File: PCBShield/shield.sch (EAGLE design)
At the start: 75 parts, among them IC1 L293D, IC3 LD117AV

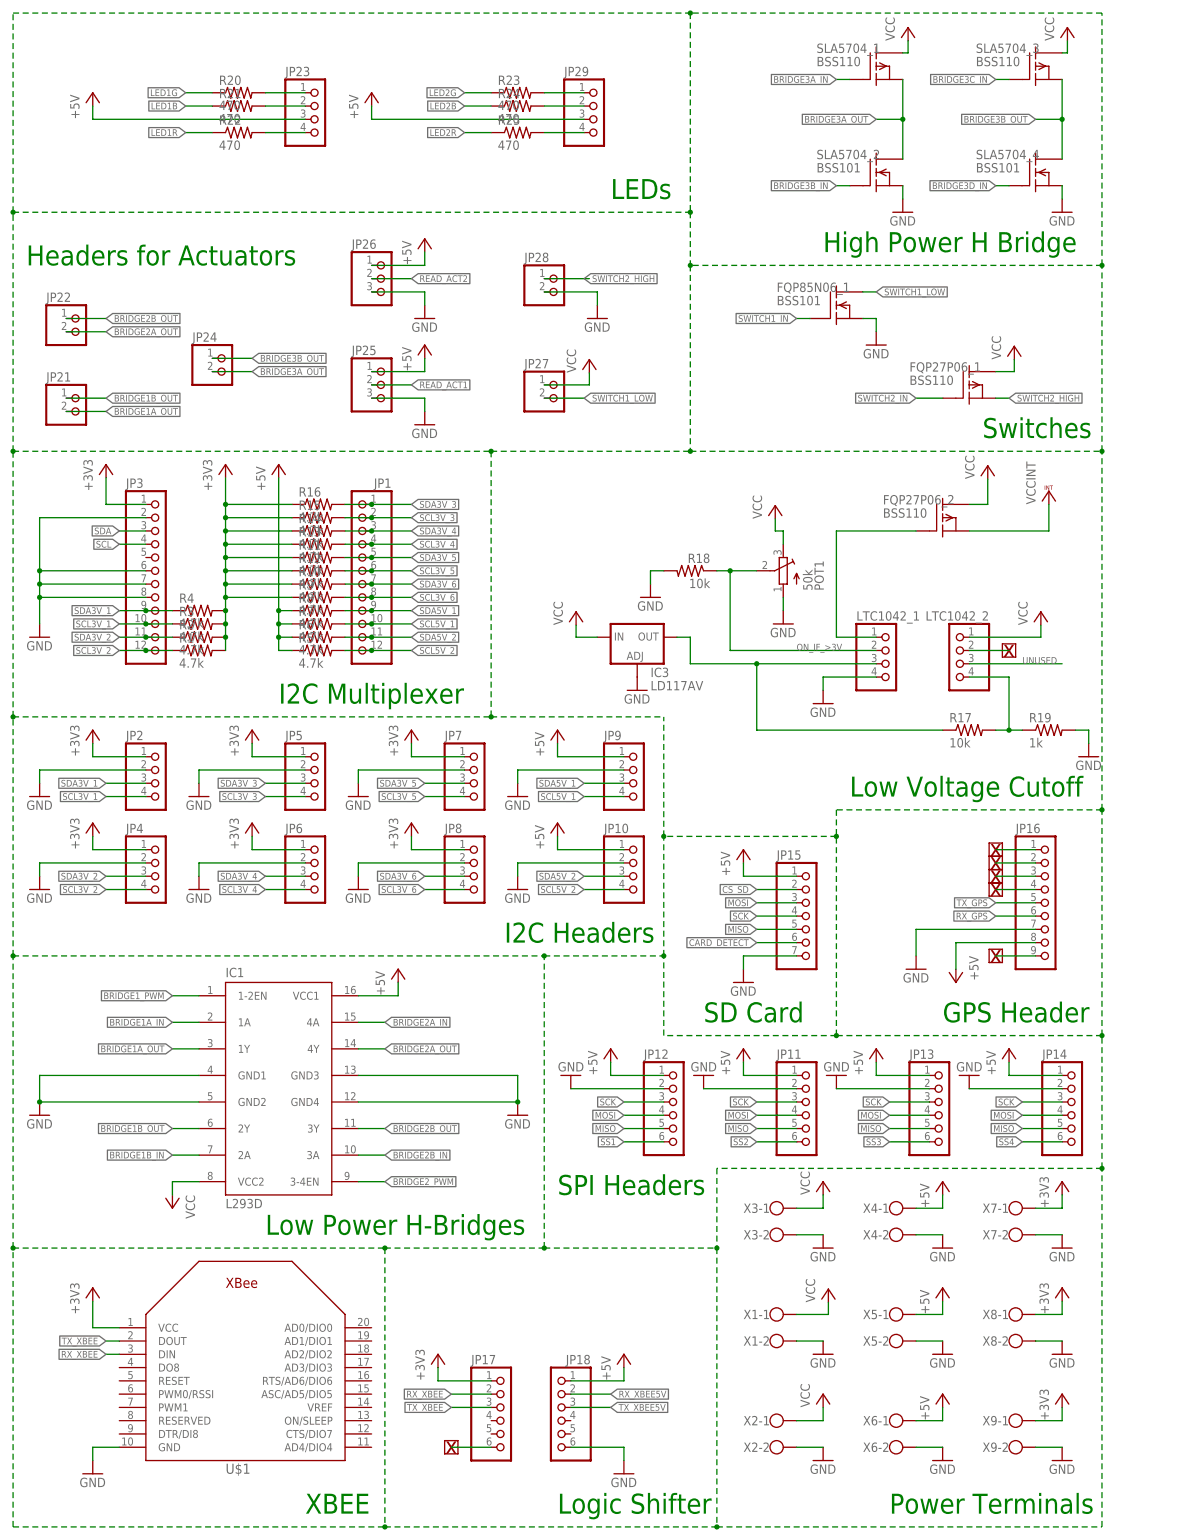
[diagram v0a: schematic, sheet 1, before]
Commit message: Now all custom parts have been created for the printed circuit board so actual board design can begin smoothly
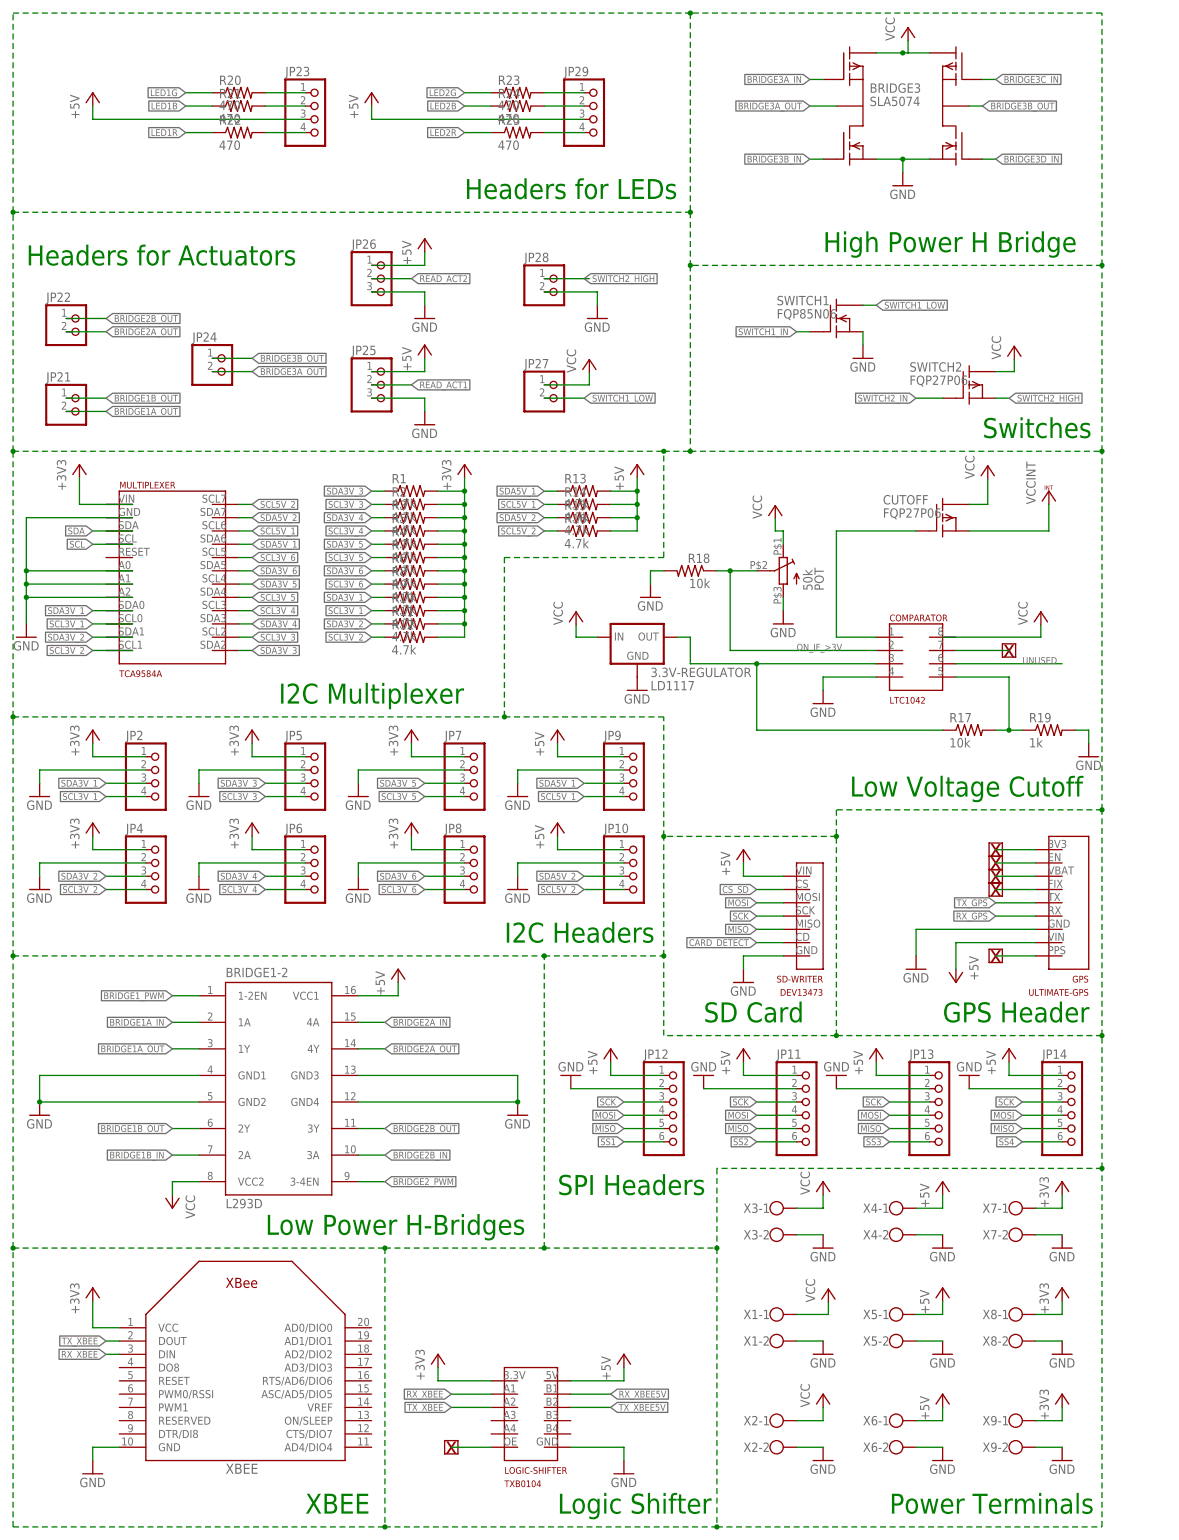
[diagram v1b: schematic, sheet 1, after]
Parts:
- removed FQP27P06_1, FQP27P06_2, SLA5704_1, SLA5704_3: BSS110, transistor-fet:BSS110
- removed FQP85N06_1, SLA5704_2, SLA5704_4: BSS101, transistor-fet:BSS101
- removed IC3: LD117AV, v-reg:LD117AV
- removed JP1, JP3: (no value), microbuilder:HEADER-1X12
- removed JP15: (no value), pinhead:PINHD-1X7
- removed JP16: (no value), pinhead:PINHD-1X9
- removed JP17, JP18: (no value), pinhead:PINHD-1X6
- removed LTC1042_1, LTC1042_2: (no value), pinhead:PINHD-1X4
- removed POT1: 50k, adafruit:TRIMPOT3386
- added 3.3V-REGULATOR: LD1117, specialparts:LD1117
- added BRIDGE3: SLA5074, specialparts:SLA5074
- added COMPARATOR: LTC1042, specialparts:LTC1042
- added CUTOFF, SWITCH2: FQP27P06, specialparts:FQP27P06
- added GPS: ULTIMATE-GPS, specialparts:ULTIMATE-GPS
- added LOGIC-SHIFTER: TXB0104, specialparts:TXB0104
- added MULTIPLEXER: TCA9584A, specialparts:TCA9584A
- added POT: 50k, specialparts:PV37W503C01B00
- added SD-WRITER: DEV13473, specialparts:DEV13473
- added SWITCH1: FQP85N06, specialparts:FQP85N06
- renumbered IC1 to BRIDGE1-2, U$1 to XBEE
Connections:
- removed net CARD_DETECT: JP15.6
- removed net N$10: JP16.2
- removed net N$11: JP16.3
- removed net N$12: JP16.4
- removed net N$13: JP17.6
- removed net N$15: LTC1042_2.2
- removed net N$17: JP16.9
- removed net N$9: JP16.1
- removed net UNUSED: LTC1042_2.3
- net +3V3: now also MULTIPLEXER.VIN, R10.2, R11.2, R12.2, R5.2, R6.2, R7.2, R8.2, R9.2; no longer JP17.1, JP3.1, R10.1, R11.1, R12.1, R13.1, R14.1, R15.1, R16.1, R9.1
- net +5V: now also R13.2, R14.2, R15.2, R16.2; no longer JP15.1, JP16.8, JP18.1, R5.1, R6.1, R7.1, R8.1
- net BRIDGE3A_IN: now also BRIDGE3.P$4; no longer SLA5704_1.G
- net BRIDGE3A_OUT: now also BRIDGE3.P$3; no longer SLA5704_1.S, SLA5704_2.D
- net BRIDGE3B_IN: now also BRIDGE3.P$2; no longer SLA5704_2.G
- net BRIDGE3B_OUT: now also BRIDGE3.P$7; no longer SLA5704_3.S, SLA5704_4.D
- net BRIDGE3C_IN: now also BRIDGE3.P$9; no longer SLA5704_3.G
- net BRIDGE3D_IN: now also BRIDGE3.P$6; no longer SLA5704_4.G
- net CS_SD: no longer JP15.2
- net GND: now also BRIDGE3.P$1, BRIDGE3.P$8, MULTIPLEXER.A0, MULTIPLEXER.A1, MULTIPLEXER.A2, MULTIPLEXER.GND, POT.P$3, SWITCH1.S; no longer FQP85N06_1.S, IC3.ADJ, JP15.7, JP16.7, JP18.6, JP3.2, JP3.6, JP3.7, JP3.8, LTC1042_1.4, POT1.A, SLA5704_2.S, SLA5704_4.S
- net MISO: no longer JP15.5
- net MOSI: no longer JP15.3
- net N$16: no longer LTC1042_2.4
- net N$18: now also CUTOFF.G; no longer FQP27P06_2.G, LTC1042_1.1
- net N$19: now also 3.3V-REGULATOR.VOUT; no longer IC3.OUT, LTC1042_1.3
- net ON_IF_>3V: now also POT.P$2; no longer LTC1042_1.2, POT1.S
- net RX_GPS: no longer JP16.6
- net RX_XBEE: no longer JP17.2
- net RX_XBEE5V: no longer JP18.2
- net SCK: no longer JP15.4
- net SCL: now also MULTIPLEXER.SCL; no longer JP3.4
- net SCL3V_1: now also MULTIPLEXER.SCL0, R10.1; no longer JP3.10, R3.1
- net SCL3V_2: now also MULTIPLEXER.SCL1, R12.1; no longer JP3.12, R1.1
- net SCL3V_3: now also R2.1; no longer JP1.2, R15.2
- net SCL3V_4: now also R5.1; no longer JP1.4, R13.2
- net SCL3V_5: now also R7.1; no longer JP1.6, R12.2
- net SCL3V_6: now also R8.1; no longer JP1.8, R9.2
- net SCL5V_1: now also R14.1; no longer JP1.10, R7.2
- net SCL5V_2: now also R16.1; no longer JP1.12, R5.2
- net SDA: now also MULTIPLEXER.SDA; no longer JP3.3
- net SDA3V_1: now also MULTIPLEXER.SDA0, R9.1; no longer JP3.9, R4.1
- net SDA3V_2: now also MULTIPLEXER.SDA1, R11.1; no longer JP3.11, R2.1
- net SDA3V_3: now also R1.1; no longer JP1.1, R16.2
- net SDA3V_4: now also R3.1; no longer JP1.3, R14.2
- net SDA3V_5: now also R4.1; no longer JP1.5, R11.2
- net SDA3V_6: now also R6.1; no longer JP1.7, R10.2
- net SDA5V_1: now also R13.1; no longer JP1.9, R8.2
- net SDA5V_2: now also R15.1; no longer JP1.11, R6.2
- net SWITCH1_IN: no longer FQP85N06_1.G
- net SWITCH1_LOW: no longer FQP85N06_1.D
- net SWITCH2_HIGH: now also SWITCH2.S; no longer FQP27P06_1.S
- net SWITCH2_IN: now also SWITCH2.G; no longer FQP27P06_1.G
- net TX_GPS: no longer JP16.5
- net TX_XBEE: no longer JP17.3
- net TX_XBEE5V: no longer JP18.3
- net VCC: now also 3.3V-REGULATOR.VIN, BRIDGE3.P$10, BRIDGE3.P$5, CUTOFF.D, POT.P$1, SWITCH2.D; no longer FQP27P06_1.D, FQP27P06_2.D, IC3.IN, LTC1042_2.1, POT1.E, SLA5704_1.D, SLA5704_3.D
- net VCCINT: now also CUTOFF.S; no longer FQP27P06_2.S
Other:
- note added: "Headers for LEDs"
- note removed: "LEDs"
- moved on the sheet: R1, R10, R11, R12, R13, R14, R15, R16, R2, R3, R4, R5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

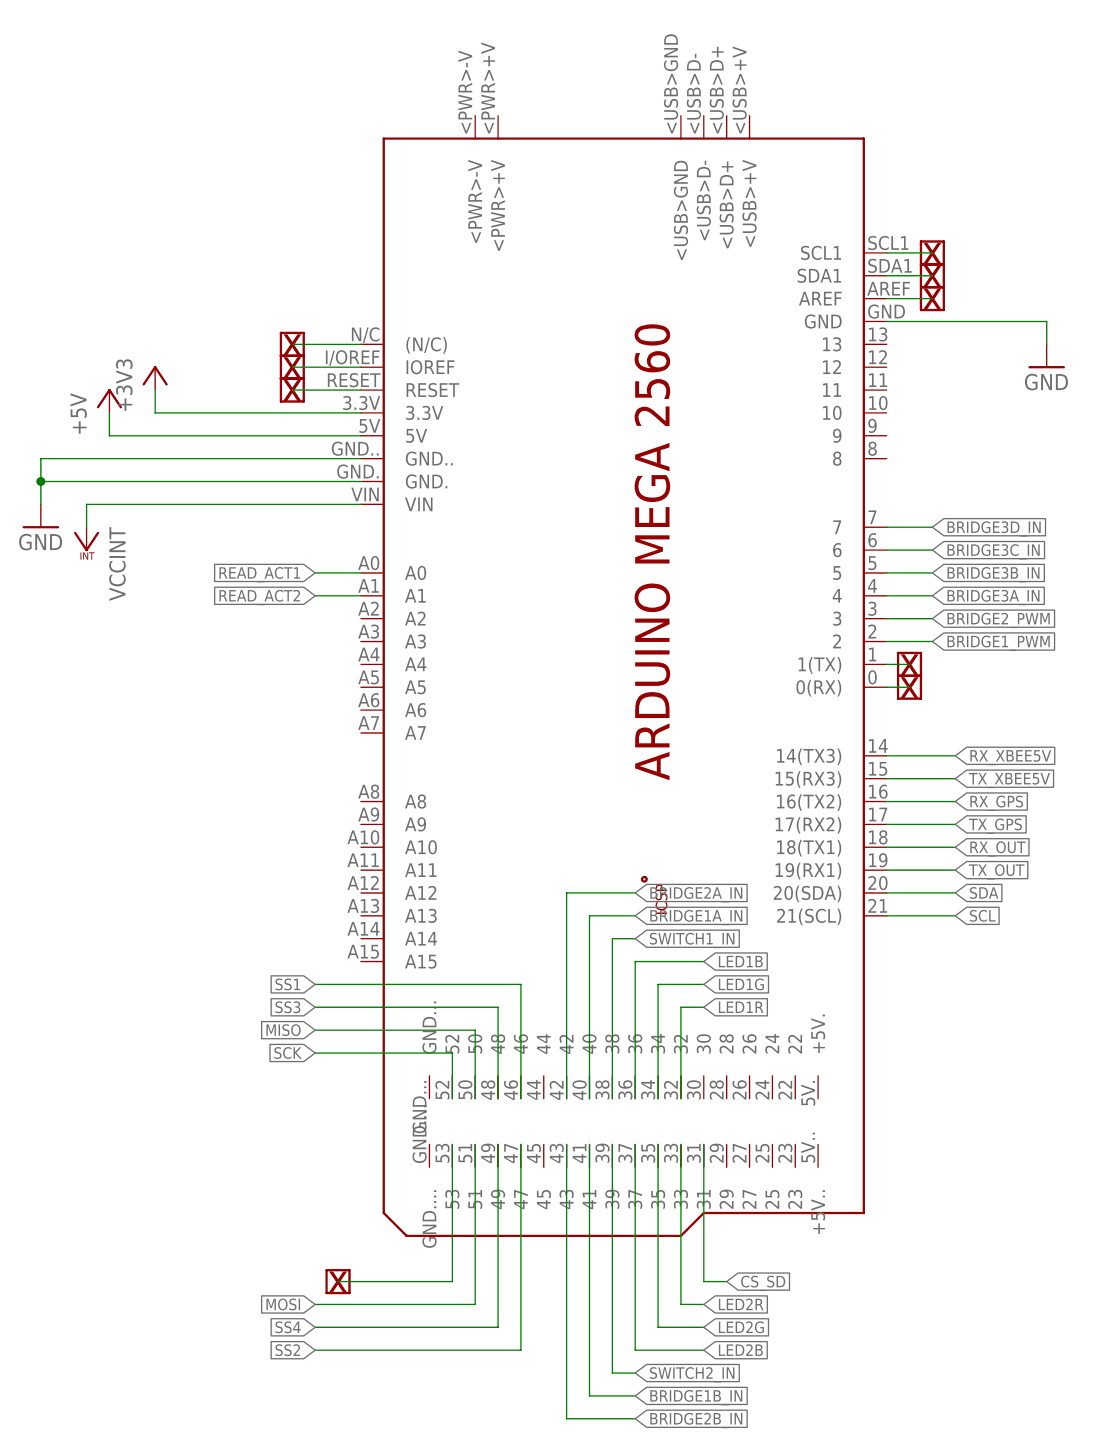
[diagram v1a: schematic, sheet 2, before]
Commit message: Revised board design to include only pins needed for a shield (no ISP header or USB/POWER). Added hole for reset switch
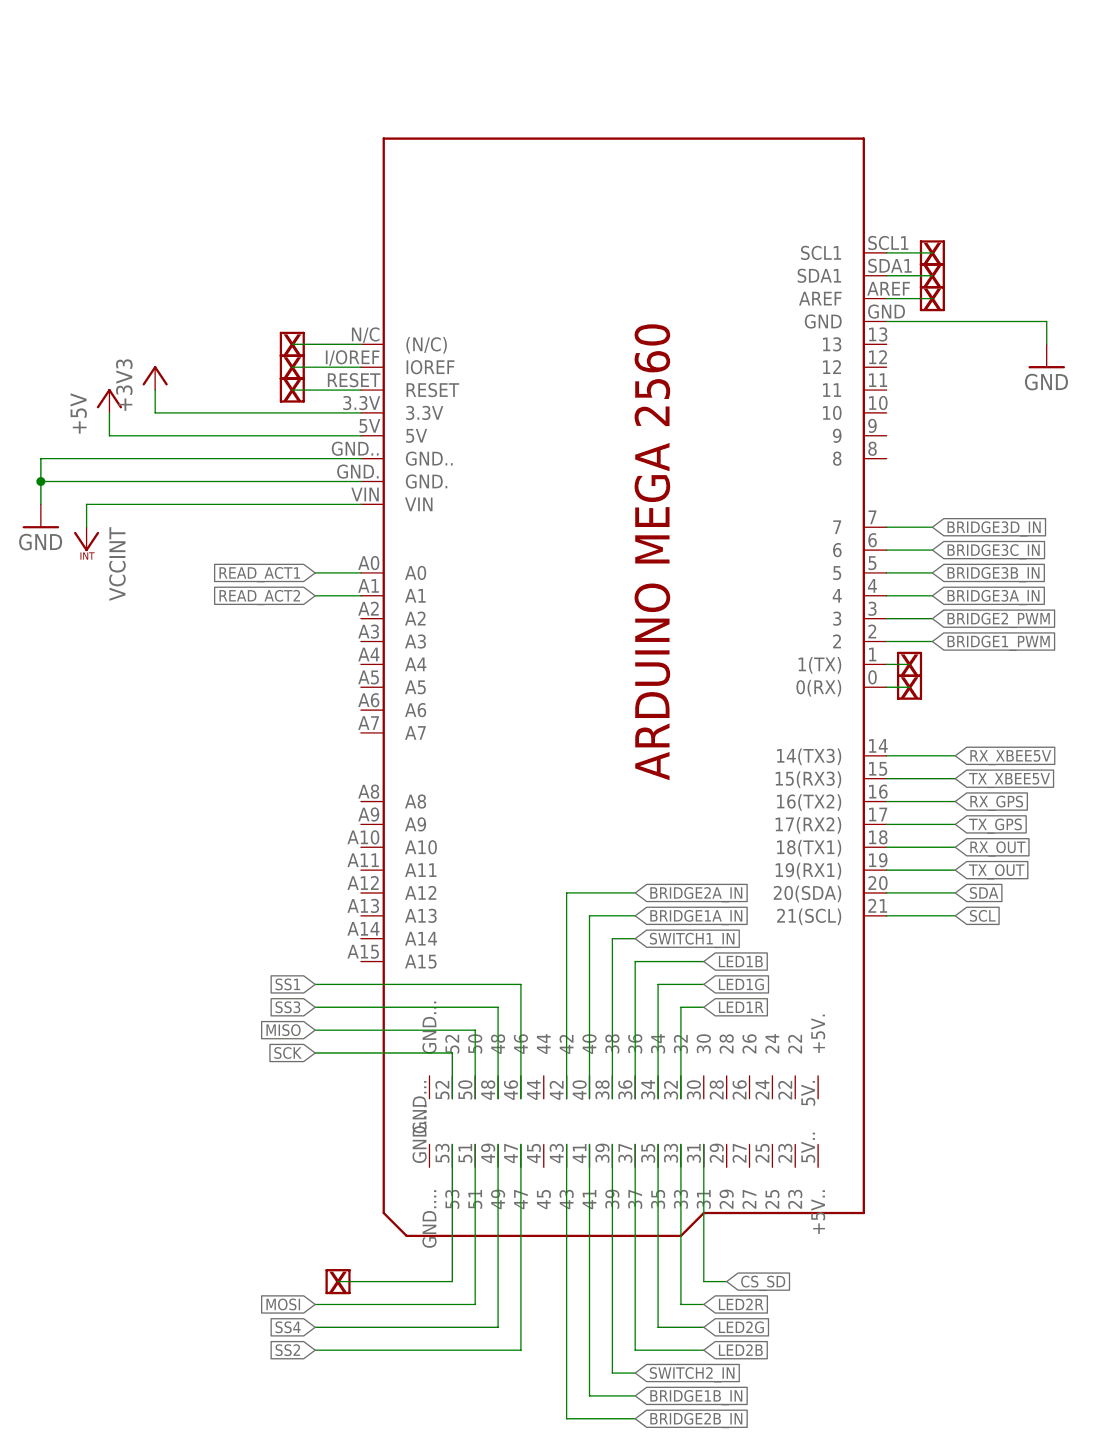
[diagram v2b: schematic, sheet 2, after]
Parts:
- removed PCB1: ARDUINO_MEGA2560, E14_Arduino_revC:ARDUINO_MEGA2560
- added PCB2: ARDUINO_MEGA2560_SHIELD, E14_Arduino_revC:ARDUINO_MEGA2560_SHIELD
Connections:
- net +3V3: now also PCB2.3.3V; no longer PCB1.3.3V
- net +5V: now also PCB2.5V; no longer PCB1.5V
- net BRIDGE1A_IN: now also PCB2.40; no longer PCB1.40
- net BRIDGE1B_IN: now also PCB2.41; no longer PCB1.41
- net BRIDGE1_PWM: now also PCB2.2; no longer PCB1.2
- net BRIDGE2A_IN: now also PCB2.42; no longer PCB1.42
- net BRIDGE2B_IN: now also PCB2.43; no longer PCB1.43
- net BRIDGE2_PWM: now also PCB2.3; no longer PCB1.3
- net BRIDGE3A_IN: now also PCB2.4; no longer PCB1.4
- net BRIDGE3B_IN: now also PCB2.5; no longer PCB1.5
- net BRIDGE3C_IN: now also PCB2.6; no longer PCB1.6
- net BRIDGE3D_IN: now also PCB2.7; no longer PCB1.7
- net CS_SD: now also PCB2.31; no longer PCB1.31
- net GND: now also PCB2.GND, PCB2.GND., PCB2.GND..; no longer PCB1.GND, PCB1.GND., PCB1.GND..
- net LED1B: now also PCB2.36; no longer PCB1.36
- net LED1G: now also PCB2.34; no longer PCB1.34
- net LED1R: now also PCB2.32; no longer PCB1.32
- net LED2B: now also PCB2.37; no longer PCB1.37
- net LED2G: now also PCB2.35; no longer PCB1.35
- net LED2R: now also PCB2.33; no longer PCB1.33
- net MISO: now also PCB2.50; no longer PCB1.50
- net MOSI: now also PCB2.51; no longer PCB1.51
- net N$2: now also PCB2.0(RX); no longer PCB1.0(RX)
- net N$3: now also PCB2.SCL1; no longer PCB1.SCL1
- net N$4: now also PCB2.SDA1; no longer PCB1.SDA1
- net N$5: now also PCB2.AREF; no longer PCB1.AREF
- net N$6: now also PCB2.(N/C); no longer PCB1.(N/C)
- net N$7: now also PCB2.IOREF; no longer PCB1.IOREF
- net N$8: now also PCB2.RESET; no longer PCB1.RESET
- net READ_ACT1: now also PCB2.A0; no longer PCB1.A0
- net READ_ACT2: now also PCB2.A1; no longer PCB1.A1
- net RESERVED: now also PCB2.1(TX); no longer PCB1.1(TX)
- net RX_GPS: now also PCB2.16(TX2); no longer PCB1.16(TX2)
- net RX_OUT: now also PCB2.18(TX1); no longer PCB1.18(TX1)
- net RX_XBEE5V: now also PCB2.14(TX3); no longer PCB1.14(TX3)
- net SCK: now also PCB2.52; no longer PCB1.52
- net SCL: now also PCB2.21(SCL); no longer PCB1.21(SCL)
- net SDA: now also PCB2.20(SDA); no longer PCB1.20(SDA)
- net SS1: now also PCB2.46; no longer PCB1.46
- net SS2: now also PCB2.47; no longer PCB1.47
- net SS3: now also PCB2.48; no longer PCB1.48
- net SS4: now also PCB2.49; no longer PCB1.49
- net SS_MASTER: now also PCB2.53; no longer PCB1.53
- net SWITCH1_IN: now also PCB2.38; no longer PCB1.38
- net SWITCH2_IN: now also PCB2.39; no longer PCB1.39
- net TX_GPS: now also PCB2.17(RX2); no longer PCB1.17(RX2)
- net TX_OUT: now also PCB2.19(RX1); no longer PCB1.19(RX1)
- net TX_XBEE5V: now also PCB2.15(RX3); no longer PCB1.15(RX3)
- net VCCINT: now also PCB2.VIN; no longer PCB1.VIN
